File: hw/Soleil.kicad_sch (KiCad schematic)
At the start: 39 parts, among them J1 Conn_01x04, Q1 Si2301, Q2 2N7002, SW1 SW_Push, U1 SPV1040TTR, U2 SPX3819M5-L-3-3, U3 STM32G030F6Px, U4 ZJY200200-0154DAAMFGN

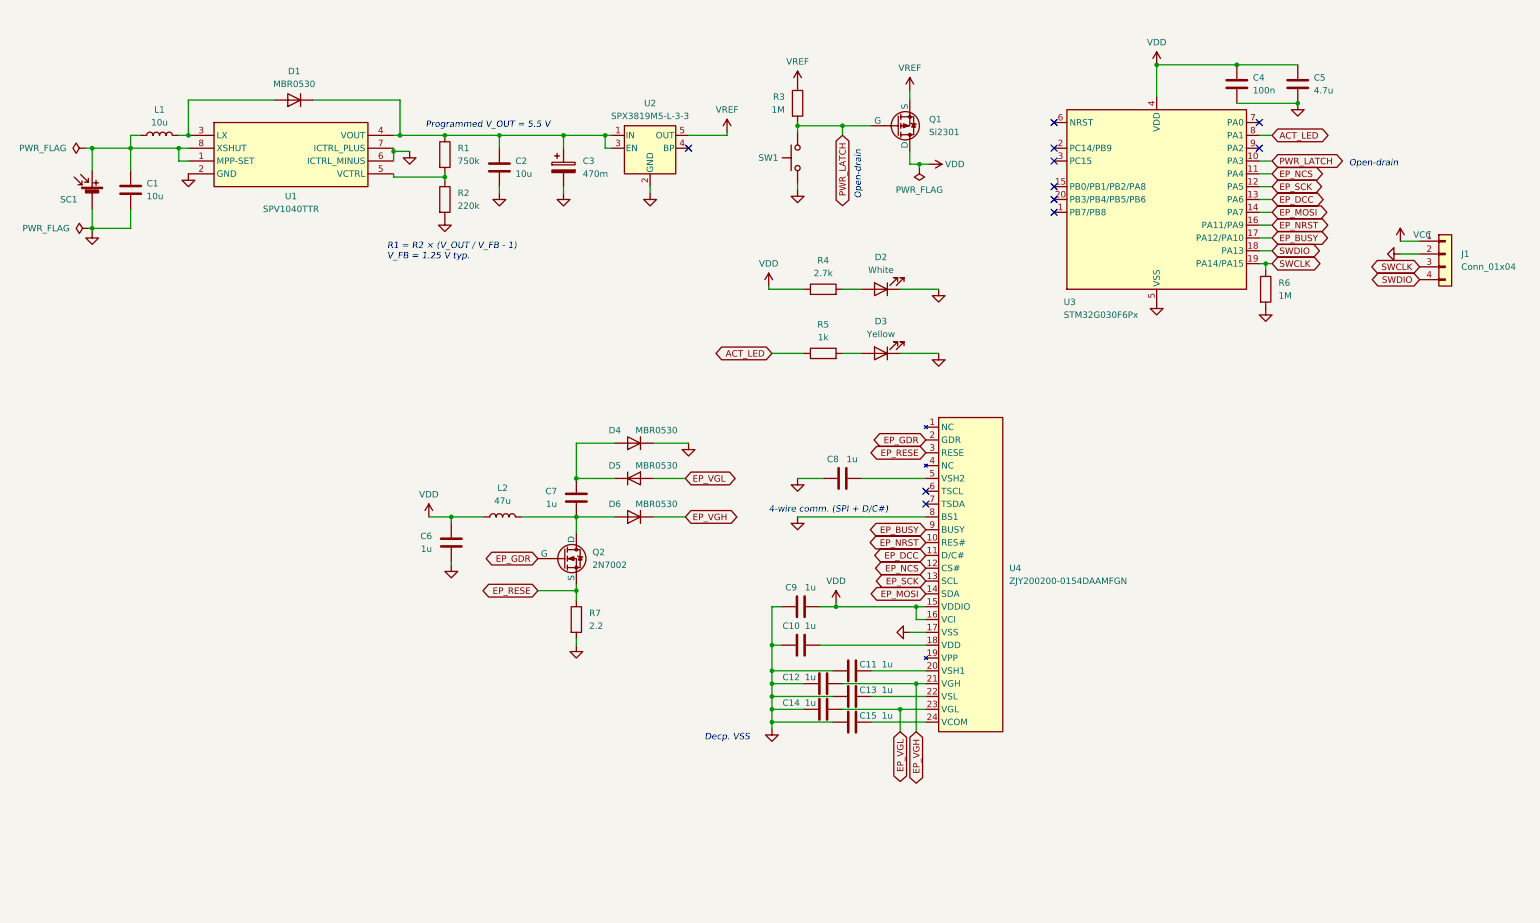
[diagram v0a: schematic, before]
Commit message: (WIP) Update PCB layout, routing to-do
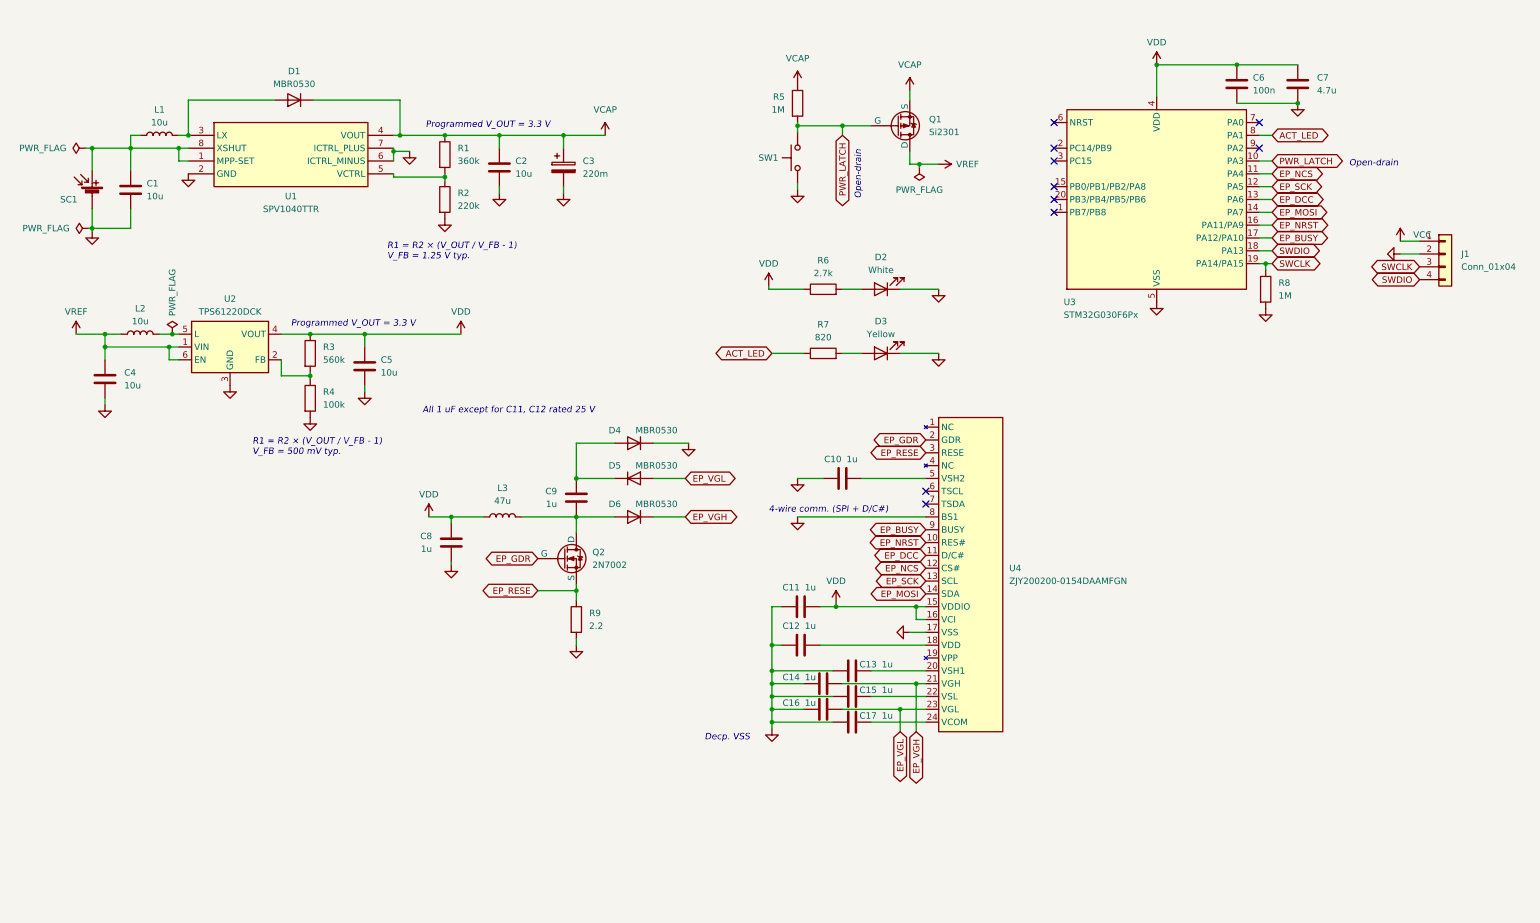
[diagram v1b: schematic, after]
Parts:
- removed U2: SPX3819M5-L-3-3, Package_TO_SOT_SMD:SOT-23-5, symbol Regulator_Linear:SPX3819M5-L-3-3
- added C4, C5: 10u, Capacitor_SMD:C_0603_1608Metric, symbol Device:C
- added L2: 10u, Inductor_SMD:L_Sunlord_SWPA252012S, symbol Device:L
- added R3: 560k, Resistor_SMD:R_0603_1608Metric, symbol Device:R
- added R4: 100k, Resistor_SMD:R_0603_1608Metric, symbol Device:R
- added U2: TPS61220DCK, Package_TO_SOT_SMD:Texas_R-PDSO-G6, symbol Regulator_Switching:TPS61220DCK
- C3: value 470m -> 220m; footprint Soleil_footprints:SuperCap_D11.5 -> Soleil_footprints:DMS3R3
- R1: value 750k -> 360k
- R7: renamed from R5; value 1k -> 820
- renumbered C8 to C10, C9 to C11, C10 to C12, C11 to C13, C12 to C14, C13 to C15, C14 to C16, C15 to C17, C4 to C6, C5 to C7, C6 to C8, C7 to C9, L2 to L3, R3 to R5, R4 to R6, R6 to R8, R7 to R9
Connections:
- net GND: now also C4.2, C5.2, R4.2, U2.3 (GND)
- net VDD: now also C5.1, R3.1, U2.4 (VOUT); no longer Q1.3 (D)
- net VREF: now also Q1.3 (D), C4.1, L2.1, U2.1 (VIN), U2.6 (EN); no longer Q1.2 (S), R5.1
- net VCAP: now reaches C2.1, C3.1, D1.1 (K), R1.1, U1.4 (VOUT)
- net VCAP: now also Q1.2 (S), R5.1
- new net: R3.2, R4.1, U2.2 (FB)
- new net: L2.2, U2.5 (L)
- no-connect marks 11 -> 10
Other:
- note added: "All 1 uF except for C11, C12 rated 25 V"
- note added: "Programmed V_OUT = 3.3 V"
- note added: "R1 = R2 × (V_OUT / V_FB - 1) V_FB = 500 mV typ."
- note removed: "Programmed V_OUT = 5.5 V"

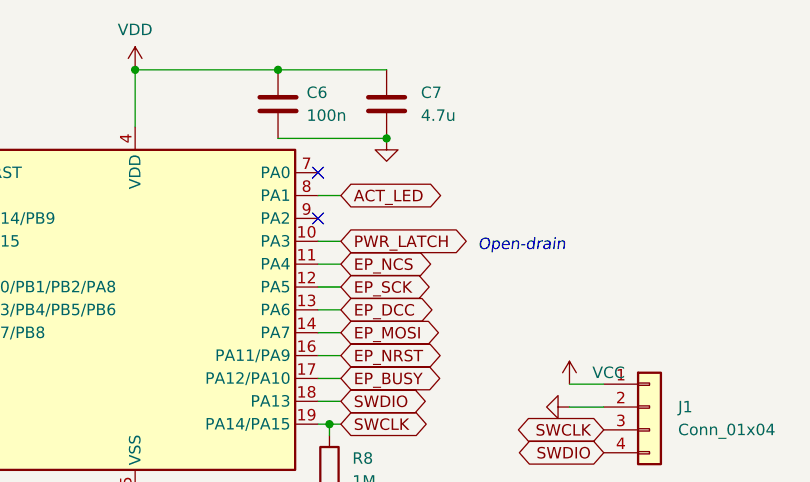
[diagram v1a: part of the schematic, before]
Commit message: Add capacitor voltage sensing
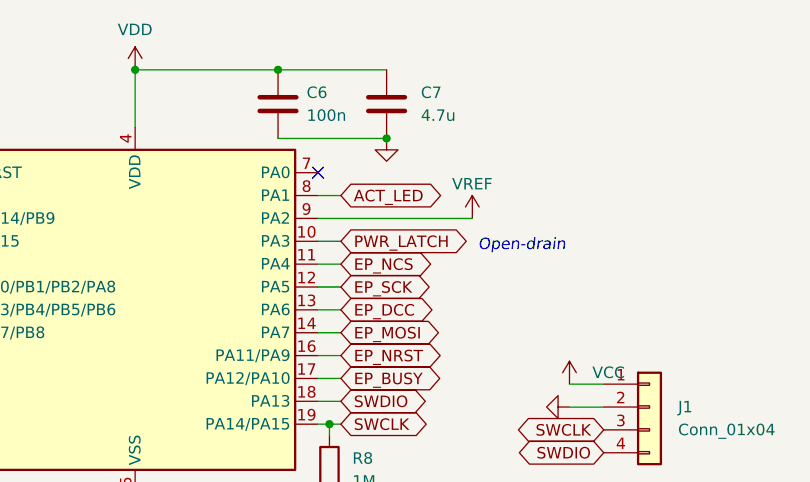
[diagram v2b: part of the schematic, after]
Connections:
- net VREF: now also U3.9 (PA2)
- no-connect marks 10 -> 9
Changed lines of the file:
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@@
   (no_connect (at 190.5 54.61))
   (no_connect (at 190.5 52.07))
-  (no_connect (at 231.14 41.91))
   (no_connect (at 190.5 49.53))
   (wire (pts (xy 2.54 81.28) (xy 15.24 81.28))
@@
   )
   (wire (pts (xy 53.975 78.74) (xy 53.975 81.28))
+    (stroke (width 0) (type default))
+  )
+  (wire (pts (xy 231.14 41.91) (xy 248.285 41.91))
     (stroke (width 0) (type default))
   )
@@
         )
       )
+    )
+  )
+  (symbol (lib_id "Soleil_symbols:VREF") (at 248.285 41.91 0) (unit 1)
+    (in_bom yes) (on_board yes) (dnp no)
+    (property "Reference" "#PWR036" (at 248.285 45.72 0)
+      (effects (font (size 1.27 1.27)) hide)
+    )
+    (property "Value" "VREF" (at 248.285 38.1 0)
+      (effects (font (size 1.27 1.27)))
+    )
+    (property "Footprint" "" (at 248.285 41.91 0)
+      (effects (font (size 1.27 1.27)) hide)
+    )
+    (property "Datasheet" "" (at 248.285 41.91 0)
+      (effects (font (size 1.27 1.27)) hide)
+    )
+    (pin "1")
+    (instances
+      (project "Soleil"
+        (path "/218ebbfa-f714-4191-a352-4c256789be77"
+          (reference "#PWR036") (unit 1)
+        )
+      )

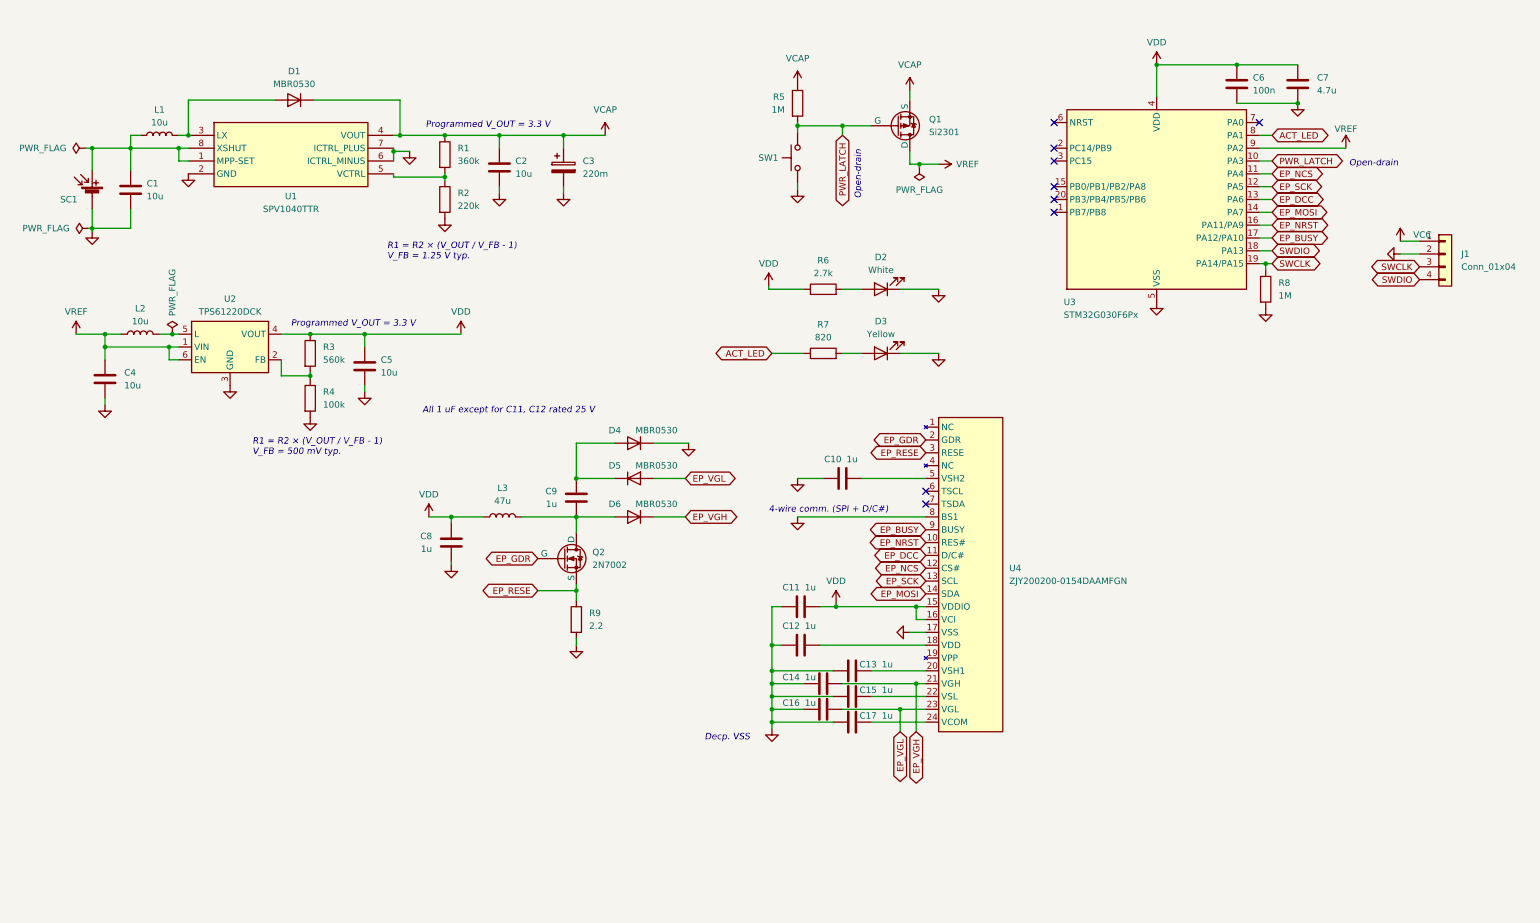
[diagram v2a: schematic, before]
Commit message: Change LED to SMD RGB; submit for fabrication
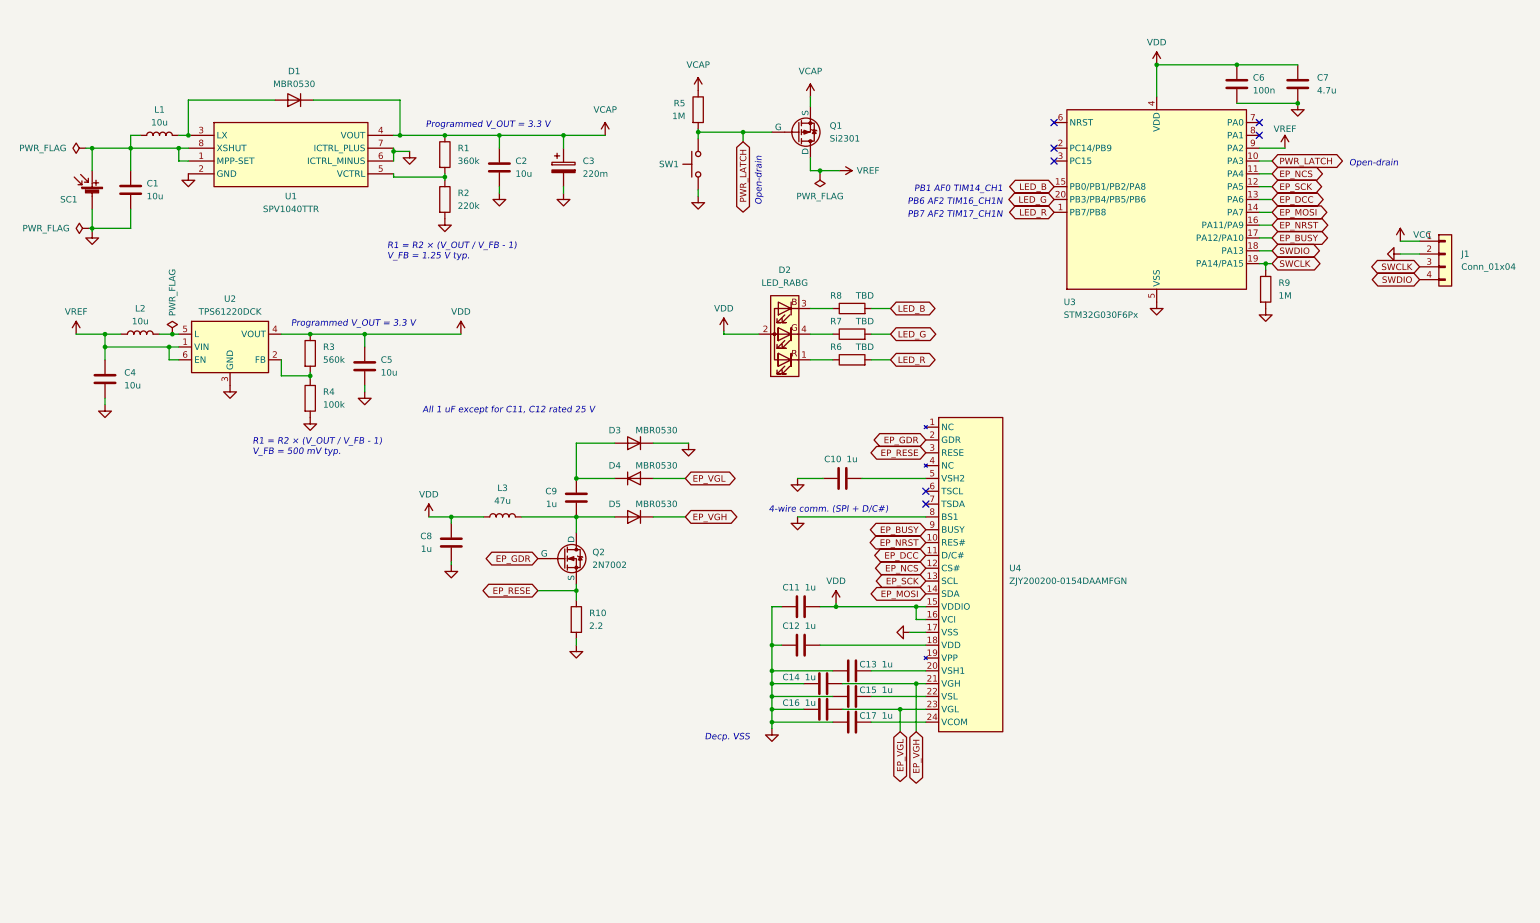
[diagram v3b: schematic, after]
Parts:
- removed D2: White, LED_SMD:LED_0603_1608Metric, symbol Device:LED
- removed D3: Yellow, LED_SMD:LED_0603_1608Metric, symbol Device:LED
- added D2: LED_RABG, LED_SMD:LED_Kingbright_AAA3528ESGCT, symbol Device:LED_RABG
- added R8: TBD, Resistor_SMD:R_0603_1608Metric, symbol Device:R
- R6: value 2.7k -> TBD
- R7: value 820 -> TBD
- renumbered D4 to D3, D5 to D4, D6 to D5, R9 to R10, R8 to R9
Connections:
- net VDD: now also D2.2 (A); no longer R6.1
- net LED_R: now reaches R6.2
- net LED_R: now also U3.1 (PB7/PB8)
- net LED_G: now reaches R7.2
- net LED_G: now also U3.20 (PB3/PB4/PB5/PB6)
- net LED_B: now reaches U3.15 (PB0/PB1/PB2/PA8)
- net LED_B: now also R8.2
- net ACT_LED: no longer names the net of U3.8 (PA1)
- net ACT_LED: no longer R7.1
- new net: D2.3 (BK), R8.1
- new net: D2.1 (RK), R6.1
- new net: D2.4 (GK), R7.1
- no-connect marks 9 -> 7
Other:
- note added: "PB1 AF0 TIM14_CH1"
- note added: "PB6 AF2 TIM16_CH1N"
- note added: "PB7 AF2 TIM17_CH1N"
- moved on the sheet: Q1, R5, SW1

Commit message: Revise schematic
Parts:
- removed D2: LED_RABG, LED_SMD:LED_Kingbright_AAA3528ESGCT, symbol Device:LED_RABG
- removed Q1: Si2301, Package_TO_SOT_SMD:SOT-23, symbol Device:Q_PMOS_GSD
- added D2: LED_RGB, Soleil_footprints:LED_BRG_KA_5050-6, symbol Soleil_symbols:LED_RGB
- renumbered Q2 to Q1
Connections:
- net VREF is gone; now on net VCAP: C4.1, L2.1, U2.1 (VIN), U2.6 (EN), U3.9 (PA2)
- net GND: now also D2.1 (BK), D2.3 (RK), D2.5 (GK)
- net LED_G: now also R6.2; no longer R7.2
- net LED_R: now also R7.2; no longer R6.2
- net at R8.1: now also D2.2 (BA)
- net at R6.1: now also D2.6 (GA)
- net at R7.1: now also D2.4 (RA)
- net PWR_LATCH renamed BTN_INTR
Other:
- note removed: "Open-drain"

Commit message: Revise circuit board design; submit for fab
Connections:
- net LED_G: now also U3.1 (PB7/PB8); no longer U3.20 (PB3/PB4/PB5/PB6)
- net LED_R: now also U3.20 (PB3/PB4/PB5/PB6); no longer U3.1 (PB7/PB8)
- net VCAP: no longer R5.1
- net VDD: now also R5.1
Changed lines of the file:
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@@
     )
   )
-  (global_label "LED_R" (shape bidirectional) (at 190.5 54.61 180) (fields_autoplaced)
+  (global_label "LED_G" (shape bidirectional) (at 190.5 54.61 180) (fields_autoplaced)
     (effects (font (size 1.27 1.27)) (justify right))
     (property "Intersheetrefs" "${INTERSHEET_REFS}" (at 180.7188 54.61 0)
@@
     )
   )
-  (global_label "LED_G" (shape bidirectional) (at 190.5 52.07 180) (fields_autoplaced)
+  (global_label "LED_R" (shape bidirectional) (at 190.5 52.07 180) (fields_autoplaced)
     (effects (font (size 1.27 1.27)) (justify right))
     (property "Intersheetrefs" "${INTERSHEET_REFS}" (at 180.7188 52.07 0)
@@
         (path "/218ebbfa-f714-4191-a352-4c256789be77"
           (reference "C13") (unit 1)
+        )
+      )
+    )
+  )
+  (symbol (lib_id "power:VDD") (at 120.015 30.48 0) (unit 1)
+    (in_bom yes) (on_board yes) (dnp no) (fields_autoplaced)
+    (property "Reference" "#PWR011" (at 120.015 34.29 0)
+      (effects (font (size 1.27 1.27)) hide)
+    )
+    (property "Value" "VDD" (at 120.015 26.035 0)
+      (effects (font (size 1.27 1.27)))
+    )
+    (property "Footprint" "" (at 120.015 30.48 0)
+      (effects (font (size 1.27 1.27)) hide)
+    )
+    (property "Datasheet" "" (at 120.015 30.48 0)
+      (effects (font (size 1.27 1.27)) hide)
+    )
+    (pin "1")
+    (instances
+      (project "Soleil"
+        (path "/218ebbfa-f714-4191-a352-4c256789be77"
+          (reference "#PWR011") (unit 1)
         )
       )
@@
         )
       )
-    )
-  )
-  (symbol (lib_id "Soleil_symbols:VCAP") (at 120.015 30.48 0) (unit 1)
-    (in_bom yes) (on_board yes) (dnp no) (fields_autoplaced)
-    (property "Reference" "#PWR011" (at 120.015 34.29 0)
-      (effects (font (size 1.27 1.27)) hide)
-    )
-    (property "Value" "VCAP" (at 120.015 25.4 0)
-      (effects (font (size 1.27 1.27)))
-    )
-    (property "Footprint" "" (at 120.015 30.48 0)
-      (effects (font (size 1.27 1.27)) hide)
-    )
-    (property "Datasheet" "" (at 120.015 30.48 0)
-      (effects (font (size 1.27 1.27)) hide)
-    )
-    (pin "1")
-    (instances
-      (project "Soleil"
-        (path "/218ebbfa-f714-4191-a352-4c256789be77"
-          (reference "#PWR011") (unit 1)
-        )
-      )
